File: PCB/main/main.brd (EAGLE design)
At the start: 49 x 50 mm, 19 parts, among them T1 2SC1815

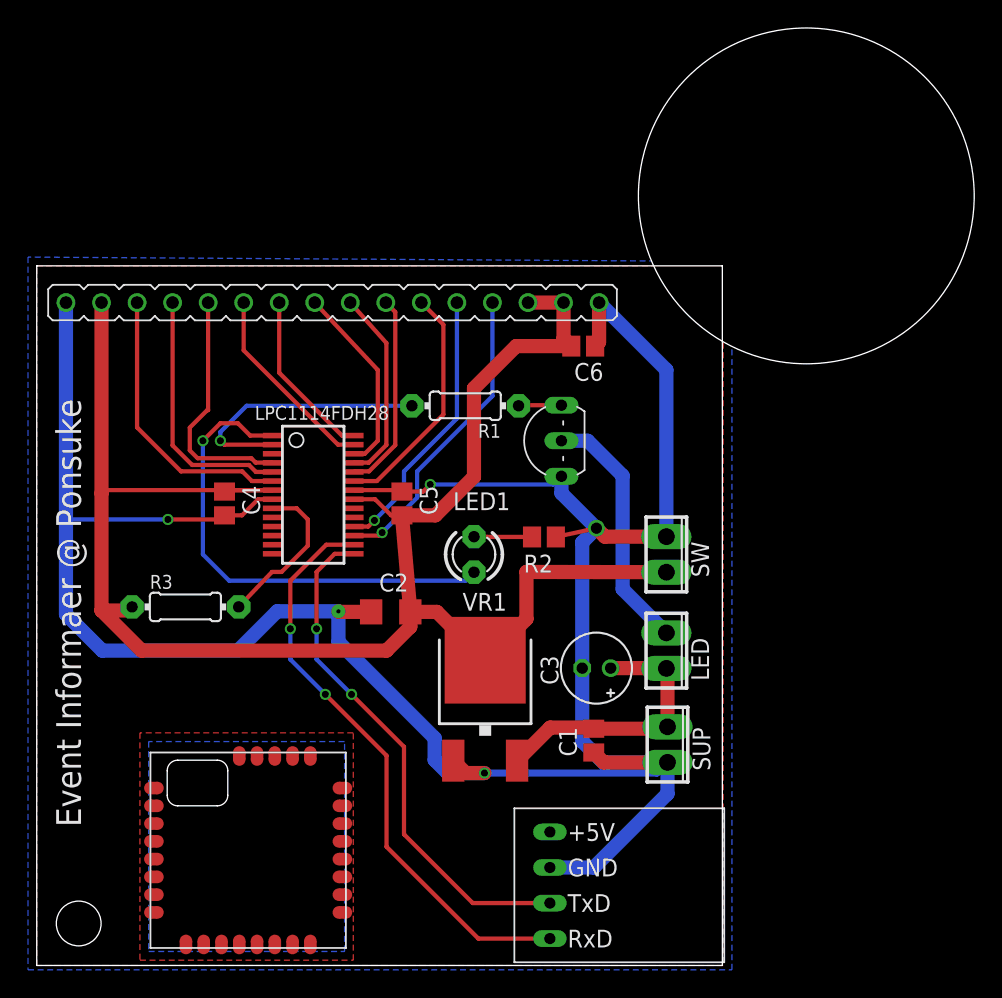
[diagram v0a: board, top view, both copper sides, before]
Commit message: PCB: Add DIP con for programing writer like isp writer.
Note that the pin assignment was modified because "reset" and"ISP Enable"
pins are required by "ISP writer" but they were used for LCD.
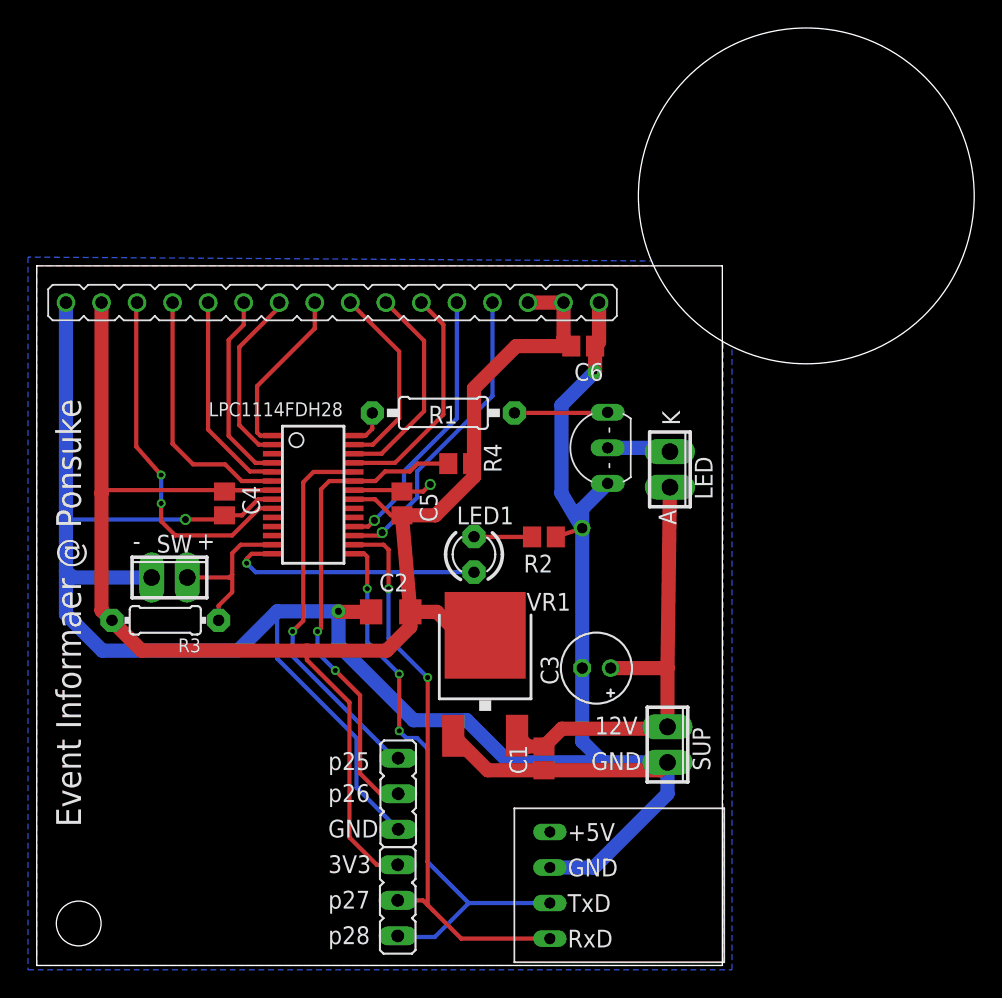
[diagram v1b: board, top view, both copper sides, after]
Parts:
- removed U$3: LITE, TWELite:LITE
- added JP1, JP2: (no value), jumper:JP2
- added R4: (no value), rcl:R2012
- R1: device rcl:0204/7 -> rcl:0207/10
- moved SW 35.6 mm to (9.49, 27.7), turned to 0 degrees
- moved LED 13.0 mm to (45.3, 35.5)
- moved C1 3.78 mm to (36.3, 14.8)
- moved T1 3.34 mm to (40.8, 37.0)
- moved VR1 1.78 mm to (32.0, 21.2)
- moved R3 1.73 mm to (9.19, 24.7), turned to 180 degrees
- moved R1 1.64 mm to (29.1, 39.5)
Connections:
- removed net N$13: R3.2, U$1.9
- new net N$1: R3.1, SW.2, U$1.13
- new net N$2: JP2.3, U$1.15, UART2USB.TXD
- new net N$3: JP2.2, U$1.16, UART2USB.RXD
- net +3V3: now also JP2.1, R3.2, R4.2; no longer R3.1, SW.2
- net GND: now also JP1.3
- net LCD0: now also U$1.26; no longer U$1.24
- net LCD1: now also U$1.27; no longer U$1.25
- net LCD2: now also U$1.1; no longer U$1.26
- net LCD3: now also U$1.2; no longer U$1.28
- net LCD4: now also U$1.4; no longer U$1.27
- net LCD5: now also U$1.5; no longer U$1.4
- net LCD6: now also U$1.6; no longer U$1.5
- net LCD7: now also U$1.9; no longer U$1.6
- net N$10: now also JP1.1, U$1.24; no longer U$1.15, UART2USB.TXD
- net N$11: now also U$1.25; no longer U$1.23
- net N$4: now also U$1.14; no longer U$1.1
- net N$8: now also U$1.28; no longer U$1.2
- net N$9: now also JP1.2, R4.1, U$1.23; no longer U$1.16, UART2USB.RXD
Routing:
- net N$2: track 0.00 -> 41.2 mm, vias 0 -> 3
- net N$3: track 0.00 -> 41.2 mm, vias 0 -> 2
- net N$8: track 18.9 -> 2.63 mm, vias 1 -> 0
- net N$4: track 34.4 -> 18.8 mm
- net N$5: track 17.9 -> 4.56 mm
- net +12V: track 20.2 -> 32.9 mm
- net N$1: track 0.00 -> 11.6 mm
- net N$13: track 11.5 -> 0.00 mm
- net N$10: track 37.0 -> 27.3 mm, vias 2 -> 1
- net GND: track 186.2 -> 193.7 mm
- net N$9: track 41.9 -> 34.9 mm
- net LCD7: track 20.2 -> 25.5 mm, vias 0 -> 2
- net N$6: track 3.08 -> 6.68 mm
- net LCD5: track 17.4 -> 14.9 mm
- net LCD2: track 13.7 -> 12.2 mm
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- removed copper zone on layer 1, net N$1
- removed copper zone on layer 16, net N$1
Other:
- board text added: "+"
- board text added: "-"
- board text added: "12V"
- board text added: "3V3"
- board text added: "A"
- board text added: "GND"
- board text added: "K"
- board text added: "p25"
- board text added: "p26"
- board text added: "p27"
- board text added: "p28"
